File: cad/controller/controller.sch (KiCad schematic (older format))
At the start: 64 parts, among them J1 RJ45_jack_POE, J2 Barrel_Jack, SW1 SW_Push, U1 NCP1117-5.0_SOT223, U2 NCP1117-3.3_SOT223, U3 CAT811STBI-GT3, U4 W5500, Y1 25MHz

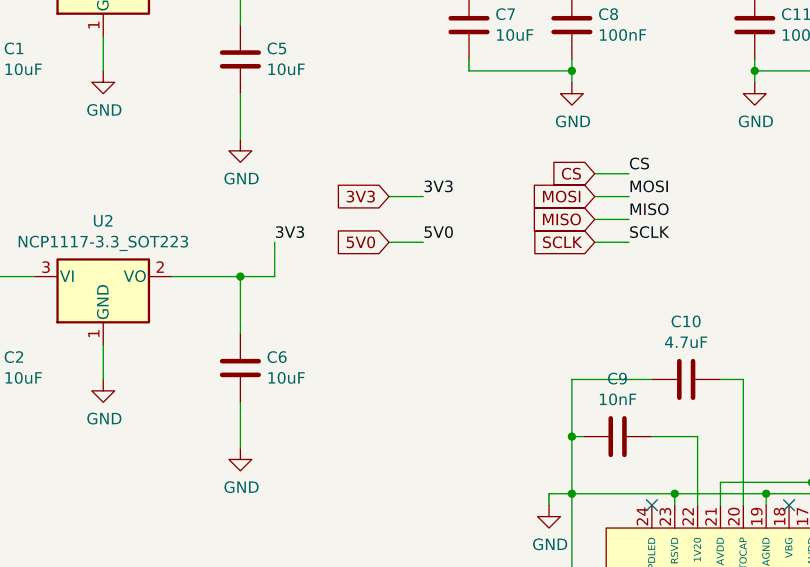
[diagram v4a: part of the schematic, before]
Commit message: Continued controller routing
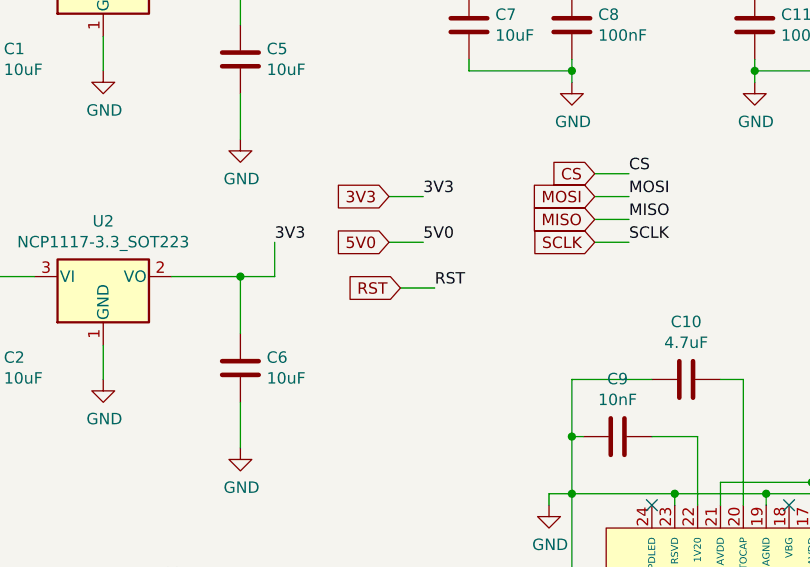
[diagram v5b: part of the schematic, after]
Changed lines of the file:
@@
 Wire Wire Line
 	9100 4450 9250 4450
+Text Label 3250 2300 0    50   ~ 0
+RST
+Text GLabel 3100 2300 0    50   Input ~ 0
+RST
+Wire Wire Line
+	3100 2300 3250 2300
 $EndSCHEMATC

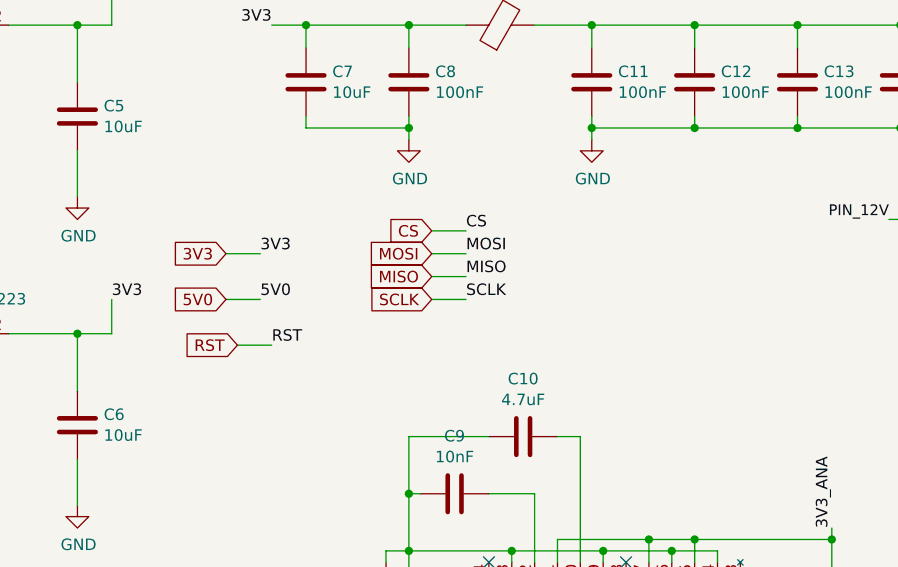
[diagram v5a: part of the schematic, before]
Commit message: Continued routing controller board
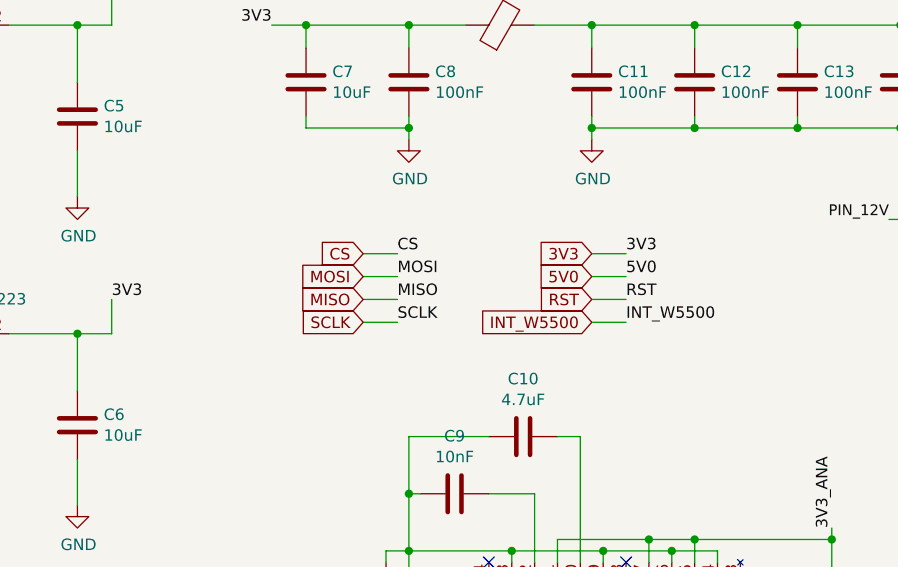
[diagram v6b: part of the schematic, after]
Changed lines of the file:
@@
 Text Label 3250 900  2    50   ~ 0
 3V3
-Text GLabel 3050 1900 0    50   Input ~ 0
+Text GLabel 4650 1900 0    50   Input ~ 0
 3V3
 Text Label 2550 2100 0    50   ~ 0
 3V3
-Text Label 3200 1900 0    50   ~ 0
+Text Label 4800 1900 0    50   ~ 0
 3V3
 Wire Wire Line
-	3050 1900 3200 1900
-Text GLabel 3050 2100 0    50   Input ~ 0
+	4650 1900 4800 1900
+Text GLabel 4650 2000 0    50   Input ~ 0
 5V0
-Text Label 3200 2100 0    50   ~ 0
+Text Label 4800 2000 0    50   ~ 0
 5V0
 Wire Wire Line
-	3050 2100 3200 2100
-Text Label 4100 2100 0    50   ~ 0
+	4650 2000 4800 2000
+Text Label 3800 2200 0    50   ~ 0
 SCLK
-Text Label 4100 2000 0    50   ~ 0
+Text Label 3800 2100 0    50   ~ 0
 MISO
-Text Label 4100 1900 0    50   ~ 0
+Text Label 3800 2000 0    50   ~ 0
 MOSI
-Text Label 4100 1800 0    50   ~ 0
+Text Label 3800 1900 0    50   ~ 0
 CS
-Text GLabel 3950 1800 0    50   Input ~ 0
+Text GLabel 3650 1900 0    50   Input ~ 0
 CS
-Text GLabel 3950 1900 0    50   Input ~ 0
+Text GLabel 3650 2000 0    50   Input ~ 0
 MOSI
-Text GLabel 3950 2000 0    50   Input ~ 0
+Text GLabel 3650 2100 0    50   Input ~ 0
 MISO
-Text GLabel 3950 2100 0    50   Input ~ 0
+Text GLabel 3650 2200 0    50   Input ~ 0
 SCLK
 Wire Wire Line
-	3950 1800 4100 1800
+	3650 1900 3800 1900
 Wire Wire Line
-	3950 1900 4100 1900
+	3650 2000 3800 2000
 Wire Wire Line
-	3950 2000 4100 2000
+	3650 2100 3800 2100
 Wire Wire Line
-	3950 2100 4100 2100
+	3650 2200 3800 2200
 Wire Wire Line
 	4650 1300 4650 1350
@@
 Wire Wire Line
 	9100 4450 9250 4450
-Text Label 3250 2300 0    50   ~ 0
+Text Label 4800 2100 0    50   ~ 0
 RST
-Text GLabel 3100 2300 0    50   Input ~ 0
+Text GLabel 4650 2100 0    50   Input ~ 0
 RST
 Wire Wire Line
-	3100 2300 3250 2300
+	4650 2100 4800 2100
+Text Label 4800 2200 0    50   ~ 0
+INT_W5500
+Text GLabel 4650 2200 0    50   Input ~ 0
+INT_W5500
+Wire Wire Line
+	4650 2200 4800 2200
 $EndSCHEMATC

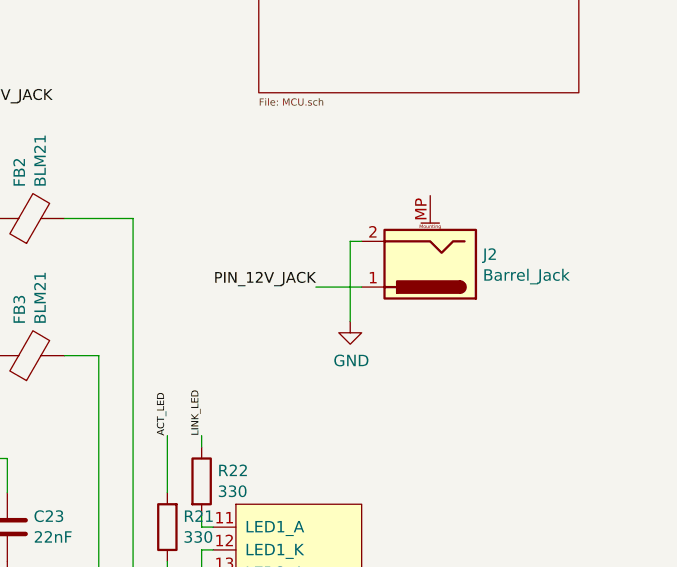
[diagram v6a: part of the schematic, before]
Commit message: Finished layout of controller (need to fix silkscreen and generate gerbers)
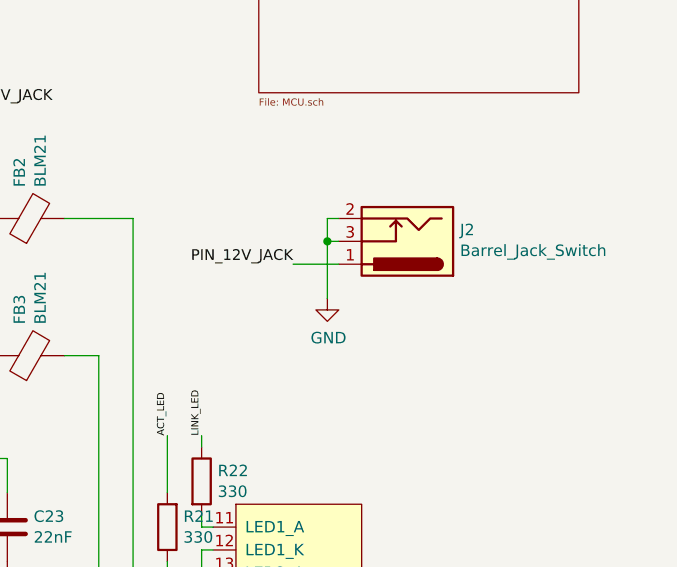
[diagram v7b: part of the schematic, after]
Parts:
- removed J2: Barrel_Jack, Connector_BarrelJack:BarrelJack_Horizontal, symbol Connector:Barrel_Jack_MountingPin
- added J2: Barrel_Jack_Switch, Connector_BarrelJack:BarrelJack_Horizontal, symbol Connector:Barrel_Jack_Switch
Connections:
- net GND: now also J2.2, J2.3
- net PIN_12V_JACK: now also J2.1
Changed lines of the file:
@@
 	-1   0    0    1
 $EndComp
-$Comp
-L Connector:Barrel_Jack_MountingPin J2
-U 1 1 6255071B
-P 10200 2450
-F 0 "J2" H 9970 2408 50  0000 R CNN
-F 1 "Barrel_Jack" H 9970 2499 50  0000 R CNN
-F 2 "Connector_BarrelJack:BarrelJack_Horizontal" H 10250 2410 50  0001 C CNN
-F 3 "~" H 10250 2410 50  0001 C CNN
-	1    10200 2450
-	-1   0    0    1
-$EndComp
-Text Label 9700 2550 2    47   ~ 0
+Text Label 9600 2450 2    47   ~ 0
 PIN_12V_JACK
 Wire Wire Line
-	9700 2550 9900 2550
-Wire Wire Line
-	9900 2350 9850 2350
-Wire Wire Line
-	9850 2350 9850 2700
+	9600 2450 9800 2450
+Wire Wire Line
+	9800 2250 9750 2250
+Wire Wire Line
+	9750 2250 9750 2350
 $Comp
 L power:GND #PWR024
 U 1 1 6259D7E2
-P 9850 2700
-F 0 "#PWR024" H 9850 2450 50  0001 C CNN
-F 1 "GND" H 9855 2527 50  0000 C CNN
-F 2 "" H 9850 2700 50  0001 C CNN
-F 3 "" H 9850 2700 50  0001 C CNN
-	1    9850 2700
+P 9750 2600
+F 0 "#PWR024" H 9750 2350 50  0001 C CNN
+F 1 "GND" H 9755 2427 50  0000 C CNN
+F 2 "" H 9750 2600 50  0001 C CNN
+F 3 "" H 9750 2600 50  0001 C CNN
+	1    9750 2600
 	1    0    0    -1
 $EndComp
@@
 Wire Wire Line
 	4650 2200 4800 2200
+$Comp
+L Connector:Barrel_Jack_Switch J2
+U 1 1 62A7274D
+P 10100 2350
+F 0 "J2" H 9870 2300 50  0000 R CNN
+F 1 "Barrel_Jack_Switch" H 9870 2391 50  0000 R CNN
+F 2 "Connector_BarrelJack:BarrelJack_Horizontal" H 10150 2310 50  0001 C CNN
+F 3 "~" H 10150 2310 50  0001 C CNN
+	1    10100 2350
+	-1   0    0    1
+$EndComp
+Wire Wire Line
+	9800 2350 9750 2350
+Connection ~ 9750 2350
+Wire Wire Line
+	9750 2350 9750 2600
 $EndSCHEMATC
